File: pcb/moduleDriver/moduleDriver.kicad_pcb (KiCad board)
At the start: 2 copper layers, 51.4 x 80 mm, 33 parts, among them J1 UART_RL, J10 Sensor, J11 Power, J12 Power, J2 UART_LR, J3 MOTOR, J4 MOTOR, J5 MOTOR, J6 MOTOR, J7 Sensor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

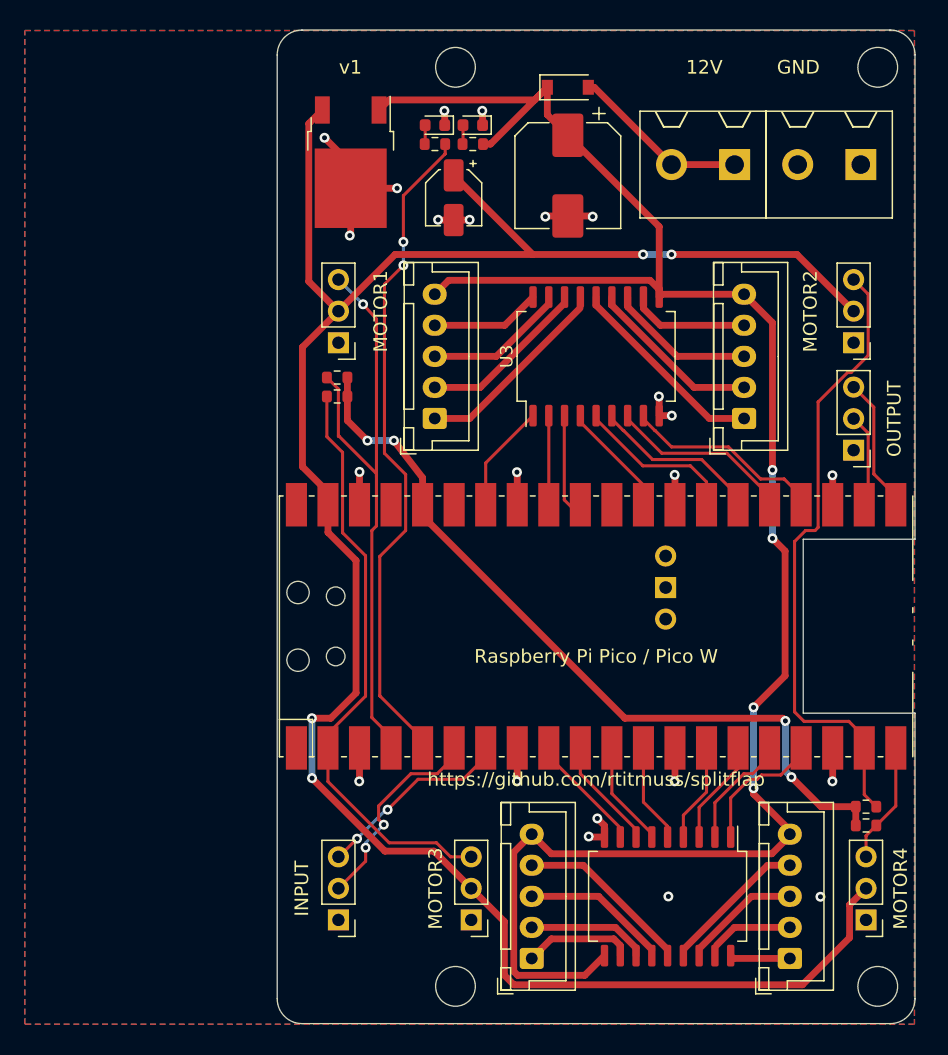
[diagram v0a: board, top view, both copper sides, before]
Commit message: Add serial resistors to uart
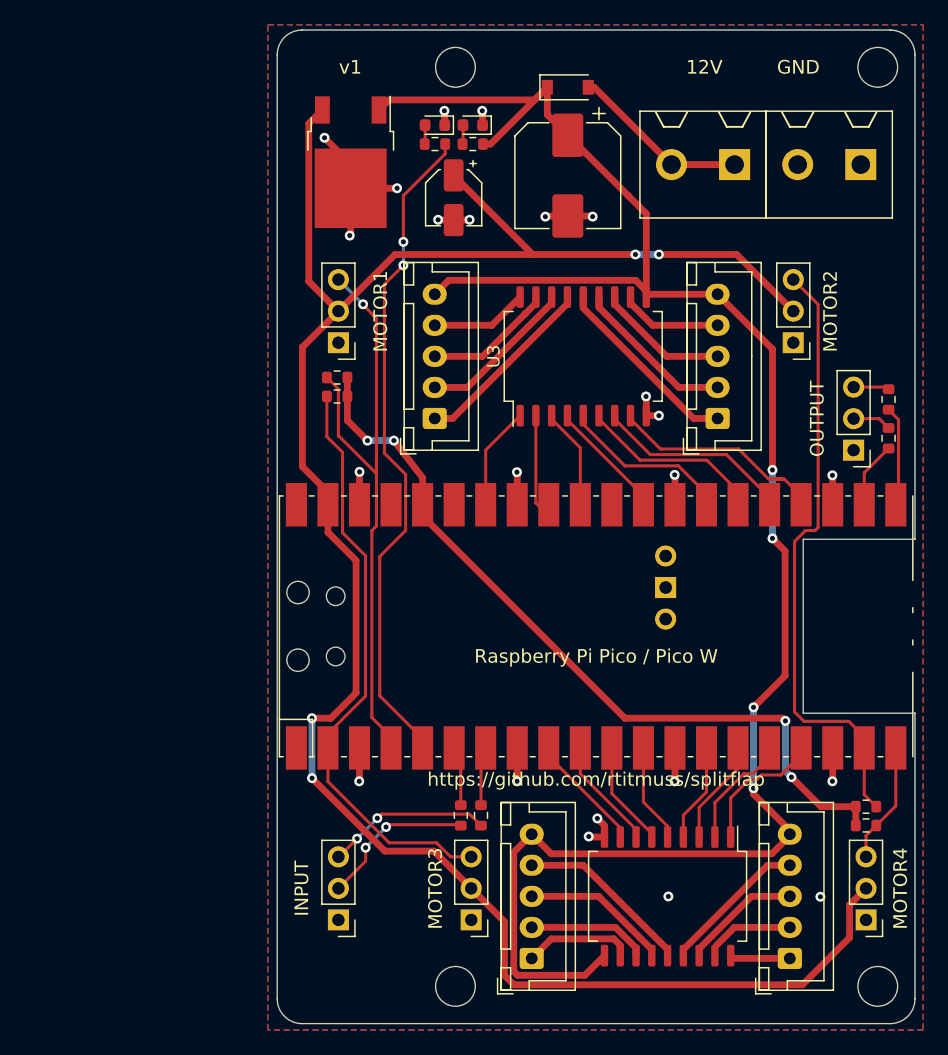
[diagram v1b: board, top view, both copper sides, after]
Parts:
- added R10: 100, Resistor_SMD:R_0603_1608Metric, F.Cu at (103.4, 113.2)
- added R7: 100, Resistor_SMD:R_0603_1608Metric, F.Cu at (137.9, 79.7)
- added R8: 100, Resistor_SMD:R_0603_1608Metric, F.Cu at (137.9, 82.9)
- added R9: 100, Resistor_SMD:R_0603_1608Metric, F.Cu at (105.1, 113.2)
- moved J7 4.86 mm to (130.2, 75.2)
- moved J4 2.13 mm to (124.1, 81.3)
- moved QR***** 1.12 mm to (113.2, 76.3)
- moved U3 1.04 mm to (113.3, 76.3)
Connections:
- J1 pad 2: /UART_RL_TX -> Net-(J1-Pad2)
- J1 pad 3: /UART_RL_RX -> Net-(J1-Pad3)
- J2 pad 2: /UART_LR_RX -> Net-(J2-Pad2)
- J2 pad 3: /UART_LR_TX -> Net-(J2-Pad3)
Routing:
- net Net-(J1-Pad3): track 0.00 -> 13.3 mm, vias 0 -> 2
- net Net-(J1-Pad2): track 0.00 -> 12.7 mm, vias 0 -> 2
- net /UART_RL_TX: track 16.0 -> 5.73 mm, vias 2 -> 0
- net /UART_RL_RX: track 15.2 -> 5.66 mm, vias 2 -> 0
- net +5V: track 171.8 -> 166.9 mm
- net /MOTOR_B_PHASE_D_P: track 15.3 -> 18.8 mm
- net /MOTOR_A_PHASE_D_P: track 7.18 -> 10.6 mm
- net /MOTOR_B_PHASE_B_P: track 12.7 -> 15.9 mm
- net Net-(J2-Pad2): track 0.00 -> 3.13 mm
- net Net-(J2-Pad3): track 0.00 -> 2.88 mm
- net /MOTOR_B_PHASE_C_P: track 14.0 -> 16.8 mm
- net /UART_LR_RX: track 8.01 -> 6.24 mm
- net +12V: track 157.6 -> 155.8 mm
- net /SENSOR_A: track 50.8 -> 49.3 mm
- net /MOTOR_B_PHASE_D: track 9.58 -> 8.24 mm
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
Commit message: Visual tweaks
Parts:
- added REF**: OSHW-Logo_5.7x6mm_SilkScreen, Symbol:OSHW-Logo_5.7x6mm_SilkScreen, F.Cu at (93.7, 126.6)

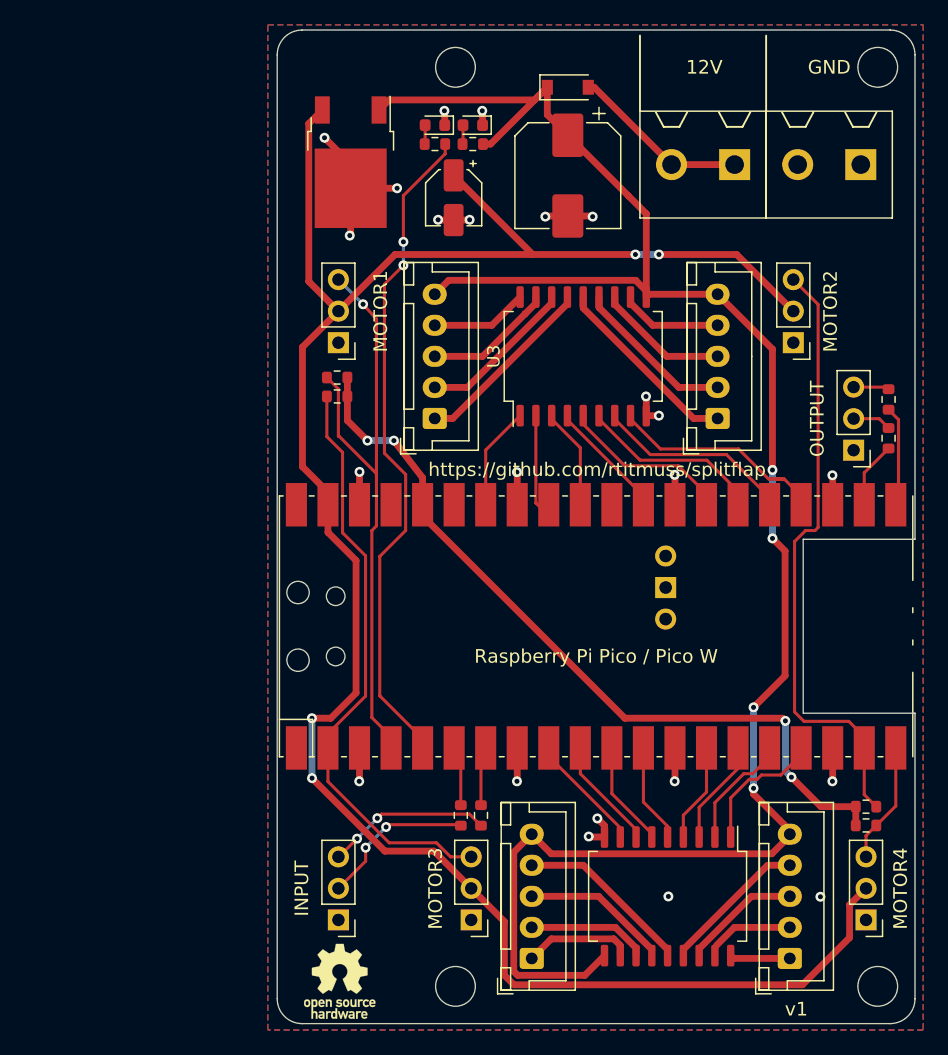
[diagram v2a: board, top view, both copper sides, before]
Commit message: Add missing gnd vias
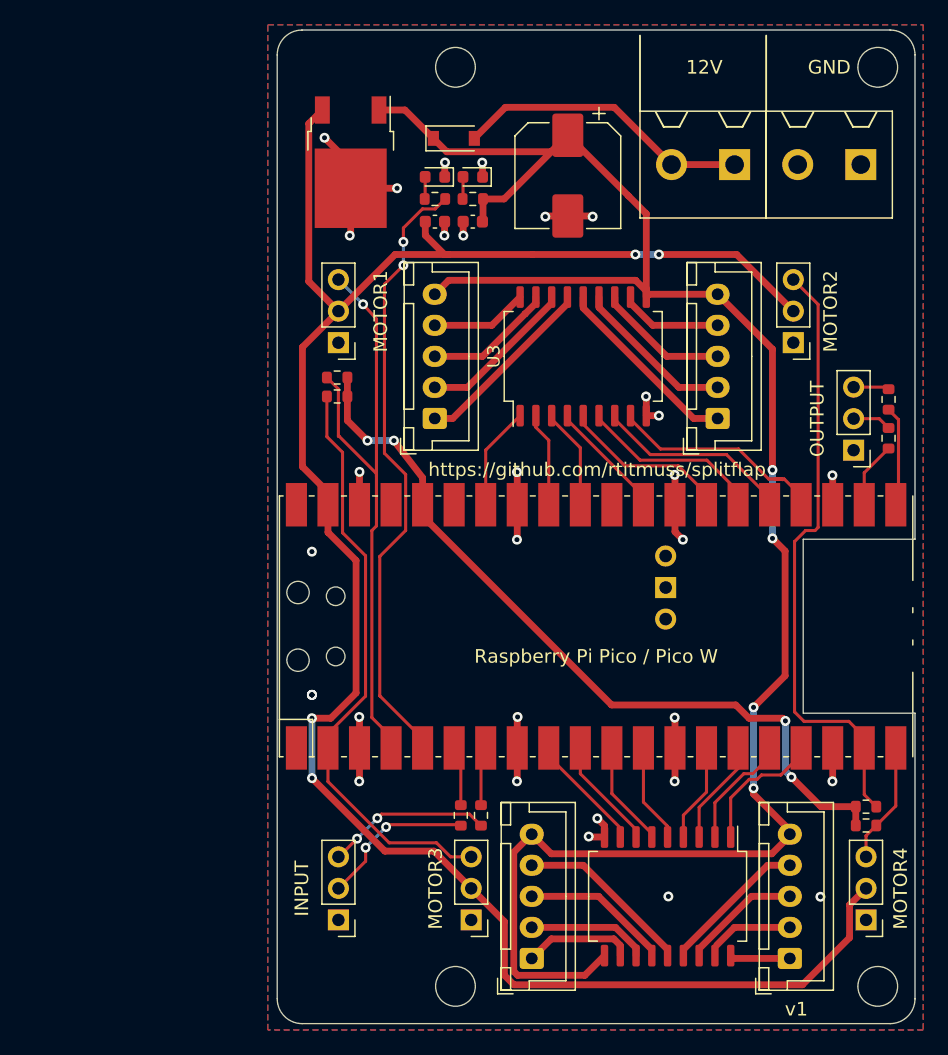
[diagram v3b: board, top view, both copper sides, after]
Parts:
- removed C4: 10uF, Capacitor_SMD:CP_Elec_4x5.3
- removed REF**: OSHW-Logo_5.7x6mm_SilkScreen, Symbol:OSHW-Logo_5.7x6mm_SilkScreen
- added C2: 0.1uF, Capacitor_SMD:C_0603_1608Metric, F.Cu at (101.3, 65.4)
- added C3: 0.1uF, Capacitor_SMD:C_0603_1608Metric, F.Cu at (104.4, 65.4)
- moved D5 10.1 mm to (102.9, 58.7)
- moved R4 4.42 mm to (101.3, 63.6)
- moved R6 4.42 mm to (104.4, 63.6)
- moved D1 4.17 mm to (101.3, 61.8)
- moved D2 4.17 mm to (104.4, 61.8)
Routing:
- net Net-(D5-Pad2): track 14.4 -> 23.9 mm
- net GND: track 52.9 -> 61.5 mm, vias 23 -> 32
- net +5V: track 166.9 -> 161.5 mm
- net /LED: track 52.7 -> 48.9 mm
- net +12V: track 155.8 -> 157.8 mm

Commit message: Silk screen fixes
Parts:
- added REF**: OSHW-Logo_5.7x6mm_SilkScreen, Symbol:OSHW-Logo_5.7x6mm_SilkScreen, F.Cu at (93.6, 126.4)
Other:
- board text added: "MODULE1"
- board text added: "MODULE2"
- board text added: "MODULE3"
- board text added: "MODULE4"
- board text removed: "MOTOR1"
- board text removed: "MOTOR2"
- board text removed: "MOTOR3"
- board text removed: "MOTOR4"

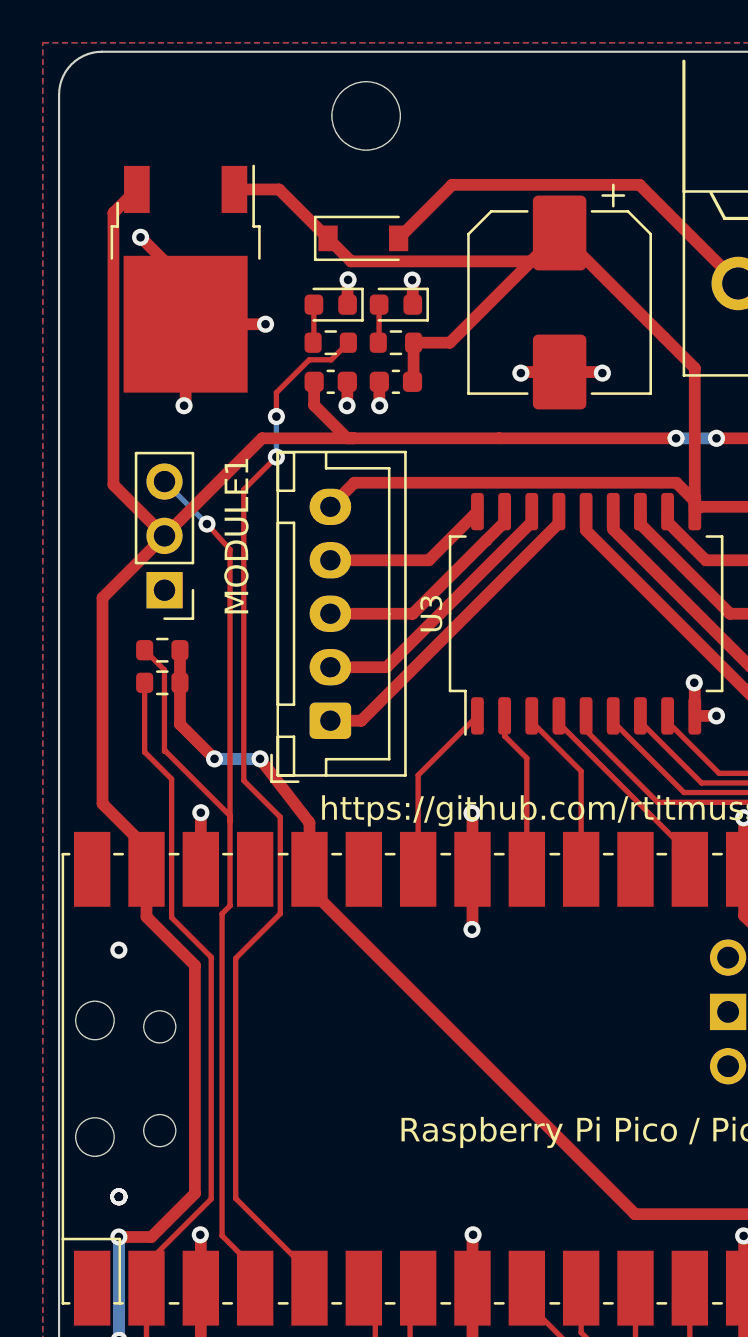
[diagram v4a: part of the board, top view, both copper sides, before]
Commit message: Move caps, add JLCJLCJLCJLC to silk screen
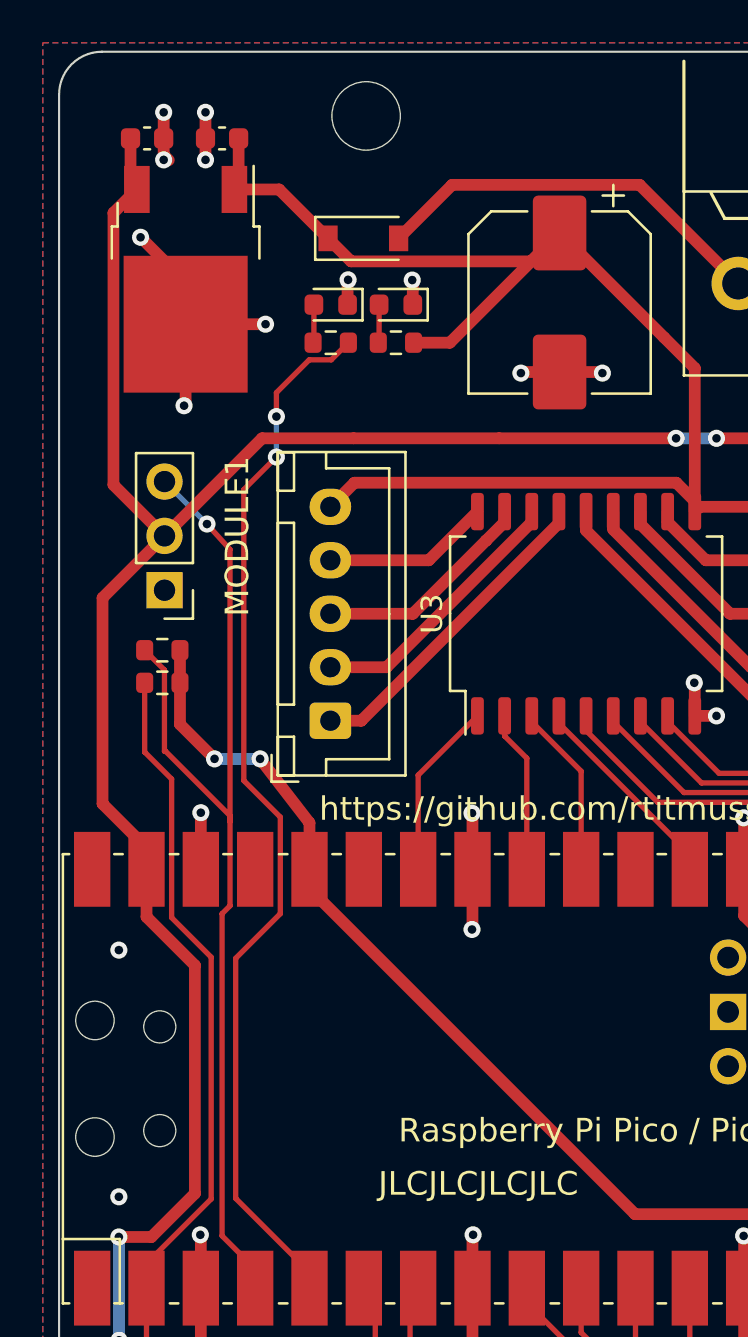
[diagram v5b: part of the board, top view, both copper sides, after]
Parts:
- moved C2 14.3 mm to (92.8, 54.1)
- moved C3 14.0 mm to (96.3, 54.1)
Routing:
- net GND: track 61.5 -> 63.8 mm
- net +5V: track 161.5 -> 160.5 mm
- net +12V: track 157.8 -> 158.5 mm
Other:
- board text added: "JLCJLCJLCJLC"

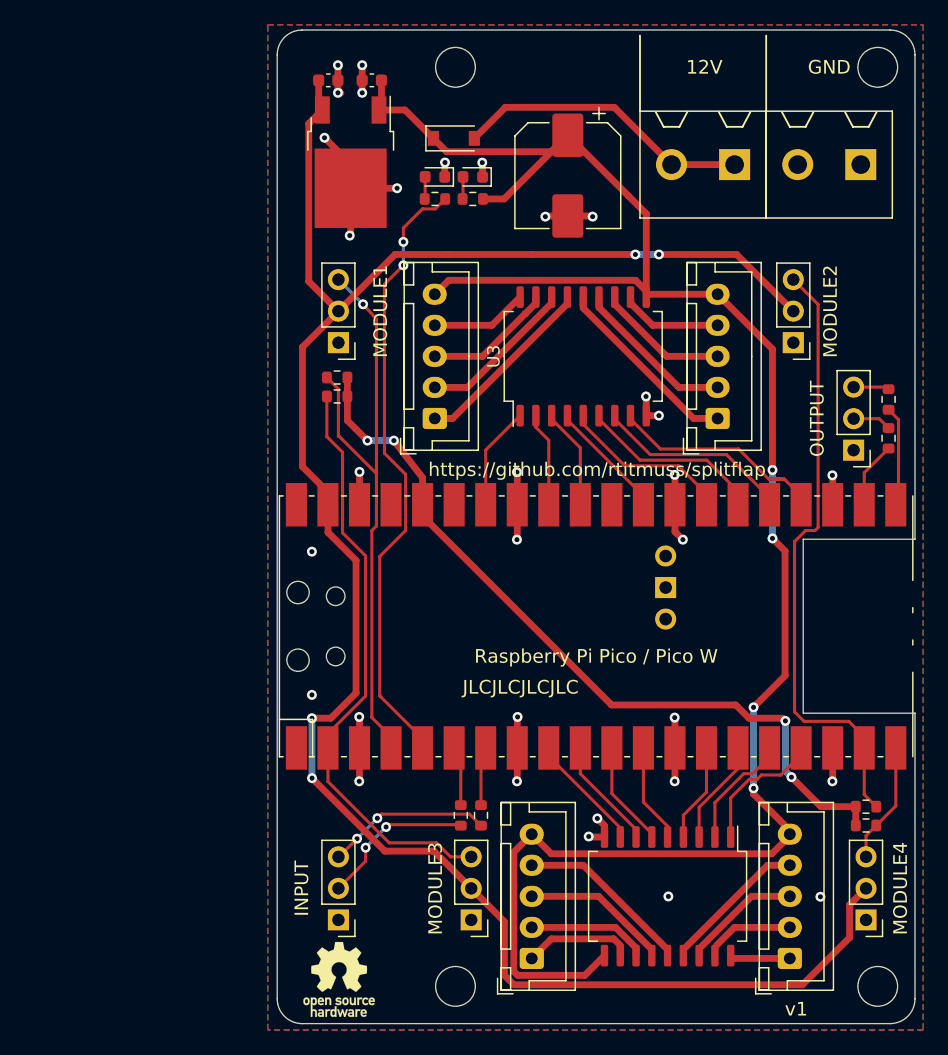
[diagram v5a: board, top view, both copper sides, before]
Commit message: Add support for neopixel
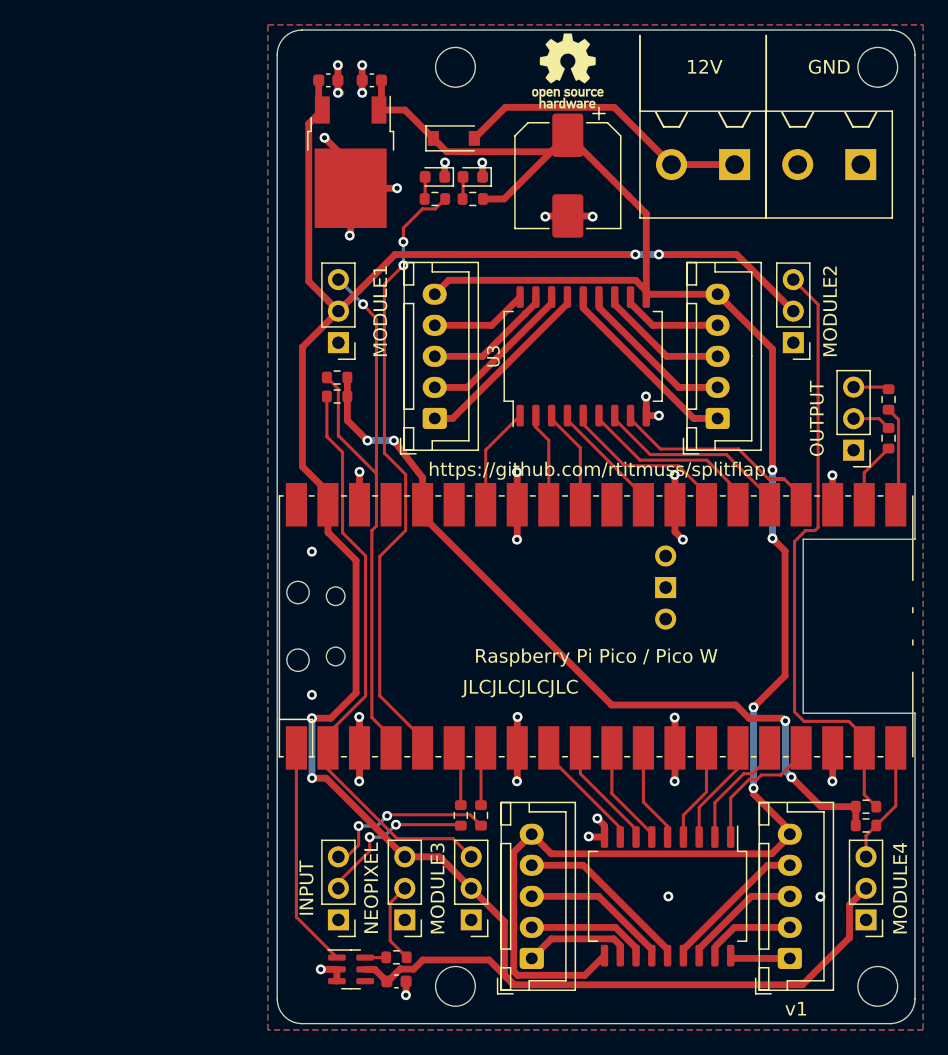
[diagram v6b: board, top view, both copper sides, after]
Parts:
- added C4: 0.1uF, Capacitor_SMD:C_0603_1608Metric, F.Cu at (98.2, 126.6)
- added J13: Neopixel, Connector_PinHeader_2.54mm:PinHeader_1x03_P2.54mm_Vertical, F.Cu at (98.9, 121.7)
- added R11: 470, Resistor_SMD:R_0603_1608Metric, F.Cu at (98.2, 124.7)
- added U5: 74HCT2G04GV, Package_SO:SC-74-6_1.5x2.9mm_P0.95mm, F.Cu at (94.6, 125.6)
- R10, R7, R8, R9: value 100 -> 470
- moved REF** 75.4 mm to (112.0, 53.3)
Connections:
- U2 pad 1: unconnected-(U2-Pad1) -> /NEOPIXEL
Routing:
- net /NEOPIXEL: track 0.00 -> 19.1 mm
- net +5V: track 160.5 -> 174.4 mm
- net Net-(J13-Pad2): track 0.00 -> 6.59 mm
- net GND: track 63.8 -> 67.2 mm, vias 32 -> 34
- net Net-(R11-Pad1): track 0.00 -> 1.70 mm
- net Net-(J1-Pad3): track 13.3 -> 14.1 mm
- net /SENSOR_C: track 47.4 -> 46.8 mm
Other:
- board text added: "NEOPIXEL"
